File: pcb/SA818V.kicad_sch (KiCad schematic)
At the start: 7 parts, among them J12 RF_SMA, Q11 BSS138, Q12 BSS138, U19 SA818S-V

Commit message: change some 0805s to 0603
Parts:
- renumbered J12 to J8, Q11 to Q13, U19 to U20
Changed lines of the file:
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@@
+			)
+		)
+		(property "Field10" ""
+			(at 135.89 113.03 0)
+			(hide yes)
+			(show_name no)
+			(do_not_autoplace no)
+			(effects
+				(font
+					(size 1.27 1.27)
+				)
 			)
 		)
@@
 		(dnp no)
 		(fields_autoplaced yes)
-		(property "Reference" "U19"
+		(property "Reference" "U20"
 			(at 140.97 54.61 0)
 			(show_name no)
@@
 		(property "Imported" "2026-09-21"
 			(at 140.97 118.11 0)
+			(hide yes)
+			(show_name no)
+			(do_not_autoplace no)
+			(effects
+				(font
+					(size 1.27 1.27)
+				)
+			)
+		)
+		(property "Field10" ""
+			(at 140.97 78.74 0)
 			(hide yes)
 			(show_name no)
@@
 			(project "foxhunt1"
 				(path "/8399ba4b-9428-480d-8b65-76cf154b97a5/249b6a5a-61a6-4c99-988d-ce75c47d35df"
-					(reference "U19")
+					(reference "U20")
 					(unit 1)
 				)
@@
 			)
 		)
+		(property "Field10" ""
+			(at 101.6 87.63 90)
+			(hide yes)
+			(show_name no)
+			(do_not_autoplace no)
+			(effects
+				(font
+					(size 1.27 1.27)
+				)
+			)
+		)
 		(pin "3"
 		)
@@
 		(dnp no)
 		(fields_autoplaced yes)
-		(property "Reference" "#PWR0166"
+		(property "Reference" "#PWR0157"
 			(at 88.9 85.09 0)
 			(hide yes)
@@
 			(project "foxhunt1"
 				(path "/8399ba4b-9428-480d-8b65-76cf154b97a5/249b6a5a-61a6-4c99-988d-ce75c47d35df"
-					(reference "#PWR0166")
+					(reference "#PWR0157")
 					(unit 1)
 				)
@@
 		(in_pos_files yes)
 		(dnp no)
-		(property "Reference" "J12"
+		(property "Reference" "J8"
 			(at 40.64 73.9531 0)
 			(show_name no)
@@
 		)
 		(property "Package" "SMA"
+			(at 44.45 74.93 0)
+			(hide yes)
+			(show_name no)
+			(do_not_autoplace no)
+			(effects
+				(font
+					(size 1.27 1.27)
+				)
+			)
+		)
+		(property "Field10" ""
 			(at 44.45 74.93 0)
 			(hide yes)
@@
 			(project "foxhunt1"
 				(path "/8399ba4b-9428-480d-8b65-76cf154b97a5/249b6a5a-61a6-4c99-988d-ce75c47d35df"
-					(reference "J12")
+					(reference "J8")
 					(unit 1)
 				)
@@
 		(dnp no)
 		(fields_autoplaced yes)
-		(property "Reference" "#PWR0160"
+		(property "Reference" "#PWR0163"
 			(at 160.02 105.41 0)
 			(hide yes)
@@
 			(project "foxhunt1"
 				(path "/8399ba4b-9428-480d-8b65-76cf154b97a5/249b6a5a-61a6-4c99-988d-ce75c47d35df"
-					(reference "#PWR0160")
+					(reference "#PWR0163")
 					(unit 1)
 				)
@@
 		(dnp no)
 		(fields_autoplaced yes)
-		(property "Reference" "#PWR0165"
+		(property "Reference" "#PWR0159"
 			(at 115.57 54.61 0)
 			(hide yes)
@@
 			(project "foxhunt1"
 				(path "/8399ba4b-9428-480d-8b65-76cf154b97a5/249b6a5a-61a6-4c99-988d-ce75c47d35df"
-					(reference "#PWR0165")
+					(reference "#PWR0159")
 					(unit 1)
 				)
@@
 		(dnp no)
 		(fields_autoplaced yes)
-		(property "Reference" "#PWR0162"
+		(property "Reference" "#PWR0160"
 			(at 116.84 123.19 0)
 			(hide yes)
@@
 			(project "foxhunt1"
 				(path "/8399ba4b-9428-480d-8b65-76cf154b97a5/249b6a5a-61a6-4c99-988d-ce75c47d35df"
-					(reference "#PWR0162")
+					(reference "#PWR0160")
 					(unit 1)
 				)
@@
 			)
 		)
+		(property "Field10" ""
+			(at 116.84 113.03 0)
+			(hide yes)
+			(show_name no)
+			(do_not_autoplace no)
+			(effects
+				(font
+					(size 1.27 1.27)
+				)
+			)
+		)
 		(pin "1"
 		)
@@
 			)
 		)
+		(property "Field10" ""
+			(at 115.57 57.15 0)
+			(hide yes)
+			(show_name no)
+			(do_not_autoplace no)
+			(effects
+				(font
+					(size 1.27 1.27)
+				)
+			)
+		)
 		(pin "1"
 		)
@@
 		(dnp no)
 		(fields_autoplaced yes)
-		(property "Reference" "#PWR0167"
+		(property "Reference" "#PWR0162"
 			(at 135.89 123.19 0)
 			(hide yes)
@@
 			(project "foxhunt1"
 				(path "/8399ba4b-9428-480d-8b65-76cf154b97a5/249b6a5a-61a6-4c99-988d-ce75c47d35df"
-					(reference "#PWR0167")
+					(reference "#PWR0162")
 					(unit 1)
 				)
@@
 		(in_pos_files yes)
 		(dnp no)
-		(property "Reference" "Q11"
+		(property "Reference" "Q13"
 			(at 105.918 57.658 90)
 			(show_name no)
@@
 		(property "Description" "50V Vds, 0.22A Id, N-Channel MOSFET, SOT-23"
 			(at 102.87 59.69 0)
+			(hide yes)
+			(show_name no)
+			(do_not_autoplace no)
+			(effects
+				(font
+					(size 1.27 1.27)
+				)
+			)
+		)
+		(property "Field10" ""
+			(at 102.87 59.69 90)
 			(hide yes)
 			(show_name no)
@@
 			(project "foxhunt1"
 				(path "/8399ba4b-9428-480d-8b65-76cf154b97a5/249b6a5a-61a6-4c99-988d-ce75c47d35df"
-					(reference "Q11")
+					(reference "Q13")
 					(unit 1)
 				)
@@
 		(dnp no)
 		(fields_autoplaced yes)
-		(property "Reference" "#PWR0163"
+		(property "Reference" "#PWR0156"
 			(at 44.45 87.63 0)
 			(hide yes)
@@
 			(project "foxhunt1"
 				(path "/8399ba4b-9428-480d-8b65-76cf154b97a5/249b6a5a-61a6-4c99-988d-ce75c47d35df"
-					(reference "#PWR0163")
+					(reference "#PWR0156")
 					(unit 1)
 				)
@@
 		(dnp no)
 		(fields_autoplaced yes)
-		(property "Reference" "#PWR0164"
+		(property "Reference" "#PWR0158"
 			(at 90.17 62.23 0)
 			(hide yes)
@@
 			(project "foxhunt1"
 				(path "/8399ba4b-9428-480d-8b65-76cf154b97a5/249b6a5a-61a6-4c99-988d-ce75c47d35df"
-					(reference "#PWR0164")
+					(reference "#PWR0158")
 					(unit 1)
 				)

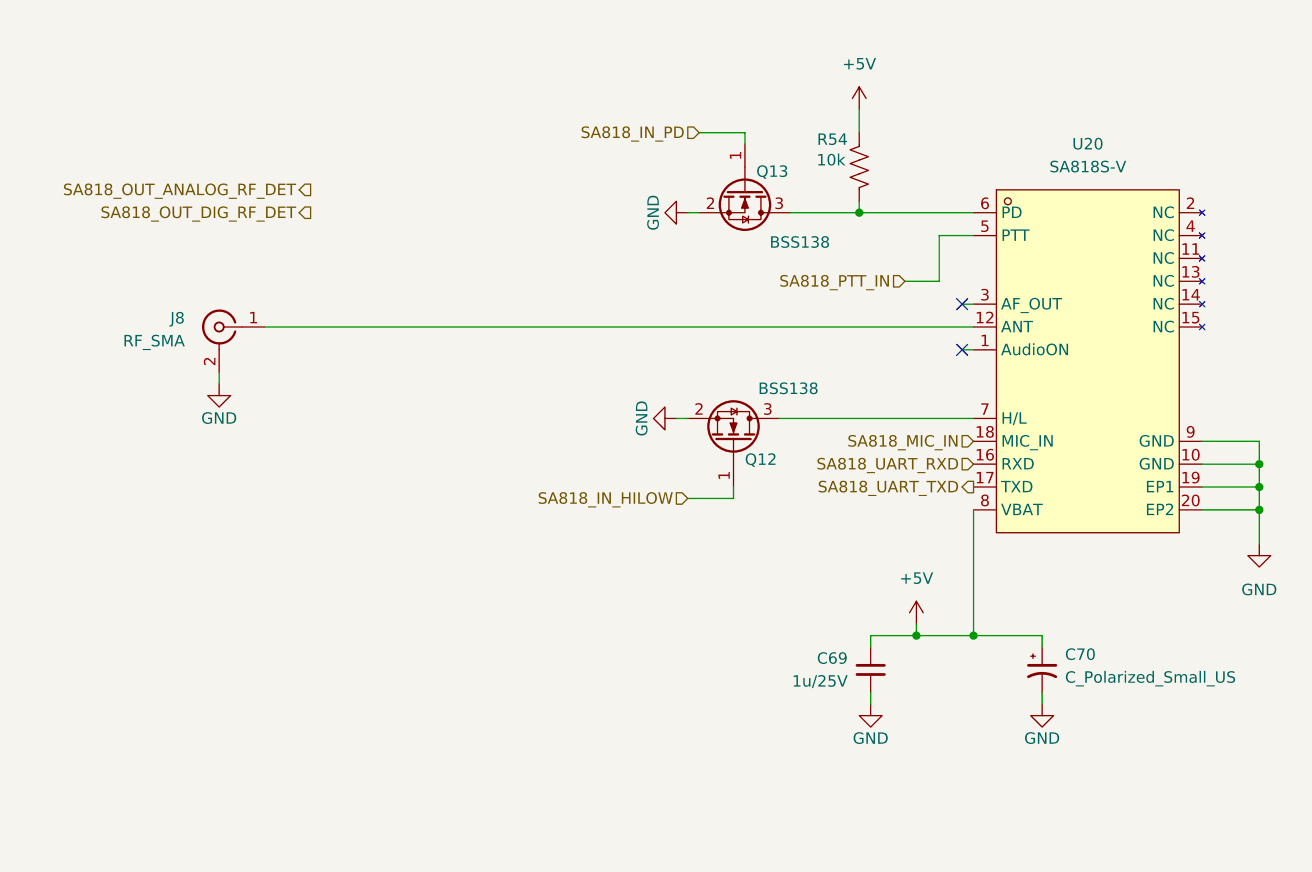
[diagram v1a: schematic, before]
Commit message: add matching network
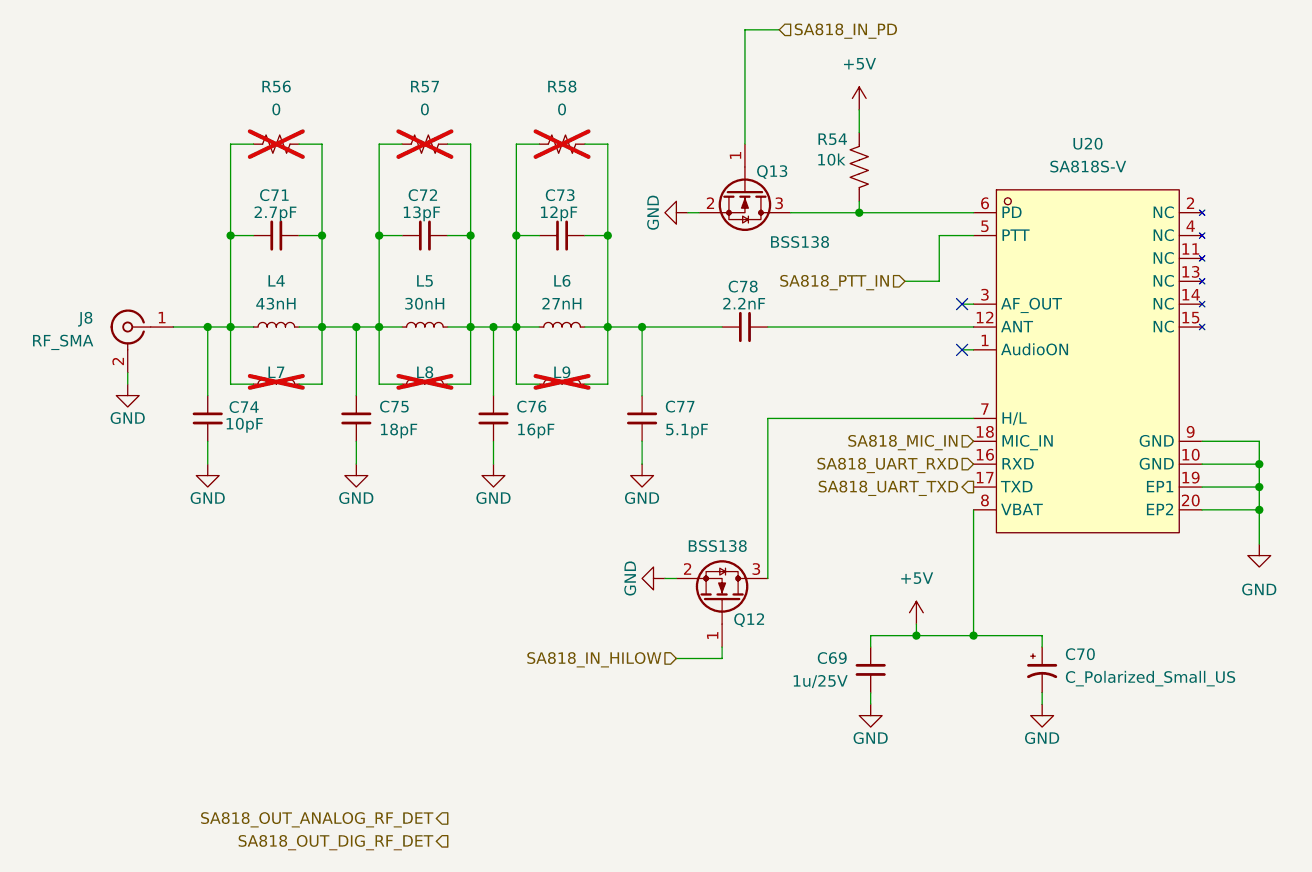
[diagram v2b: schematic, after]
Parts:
- added C71: 2.7pF, Capacitor_SMD:C_0603_1608Metric_Pad1.08x0.95mm_HandSolder, symbol Device:C_Small
- added C72: 13pF, Capacitor_SMD:C_0201_0603Metric_Pad0.64x0.40mm_HandSolder, symbol Device:C_Small
- added C73: 12pF, Capacitor_SMD:C_0603_1608Metric_Pad1.08x0.95mm_HandSolder, symbol Device:C_Small
- added C74: 10pF, Capacitor_SMD:C_0603_1608Metric_Pad1.08x0.95mm_HandSolder, symbol Device:C_Small
- added C75: 18pF, Capacitor_SMD:C_0603_1608Metric_Pad1.08x0.95mm_HandSolder, symbol Device:C_Small
- added C76: 16pF, Capacitor_SMD:C_0603_1608Metric_Pad1.08x0.95mm_HandSolder, symbol Device:C_Small
- added C77: 5.1pF, Capacitor_SMD:C_0603_1608Metric_Pad1.08x0.95mm_HandSolder, symbol Device:C_Small
- added C78: 2.2nF, Capacitor_SMD:C_0603_1608Metric_Pad1.08x0.95mm_HandSolder, symbol Device:C_Small
- added L4: 43nH, Inductor_SMD:L_0805_2012Metric_Pad1.05x1.20mm_HandSolder, symbol Device:L_Small
- added L5: 30nH, Inductor_SMD:L_0805_2012Metric_Pad1.05x1.20mm_HandSolder, symbol Device:L_Small
- added L6: 27nH, Inductor_SMD:L_0805_2012Metric_Pad1.05x1.20mm_HandSolder, symbol Device:L_Small
- added L7, L8, L9: (no value), Inductor_SMD:L_0603_1608Metric, symbol Device:L_Small
- added R56, R57, R58: 0, Resistor_THT:R_Array_SIP4, symbol Device:R_Small_US
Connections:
- net GND: now also C74.1, C75.1, C76.1, C77.1
- net at U20.12 (ANT): now also C78.2; no longer J8.1 (In)
- new net: C72.2, C73.1, C76.2, L5.2, L6.1, L8.2, L9.1, R57.2, R58.1
- new net: C71.1, C74.2, J8.1 (In), L4.1, L7.1, R56.1
- new net: C71.2, C72.1, C75.2, L4.2, L5.1, L7.2, L8.1, R56.2, R57.1
- new net: C73.2, C77.2, C78.1, L6.2, L9.2, R58.2
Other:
- moved on the sheet: J8, Q12
